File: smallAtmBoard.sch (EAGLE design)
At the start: 19 parts, among them IC1 ATMEGA-328P, IC2 7805, Y1 16MHz

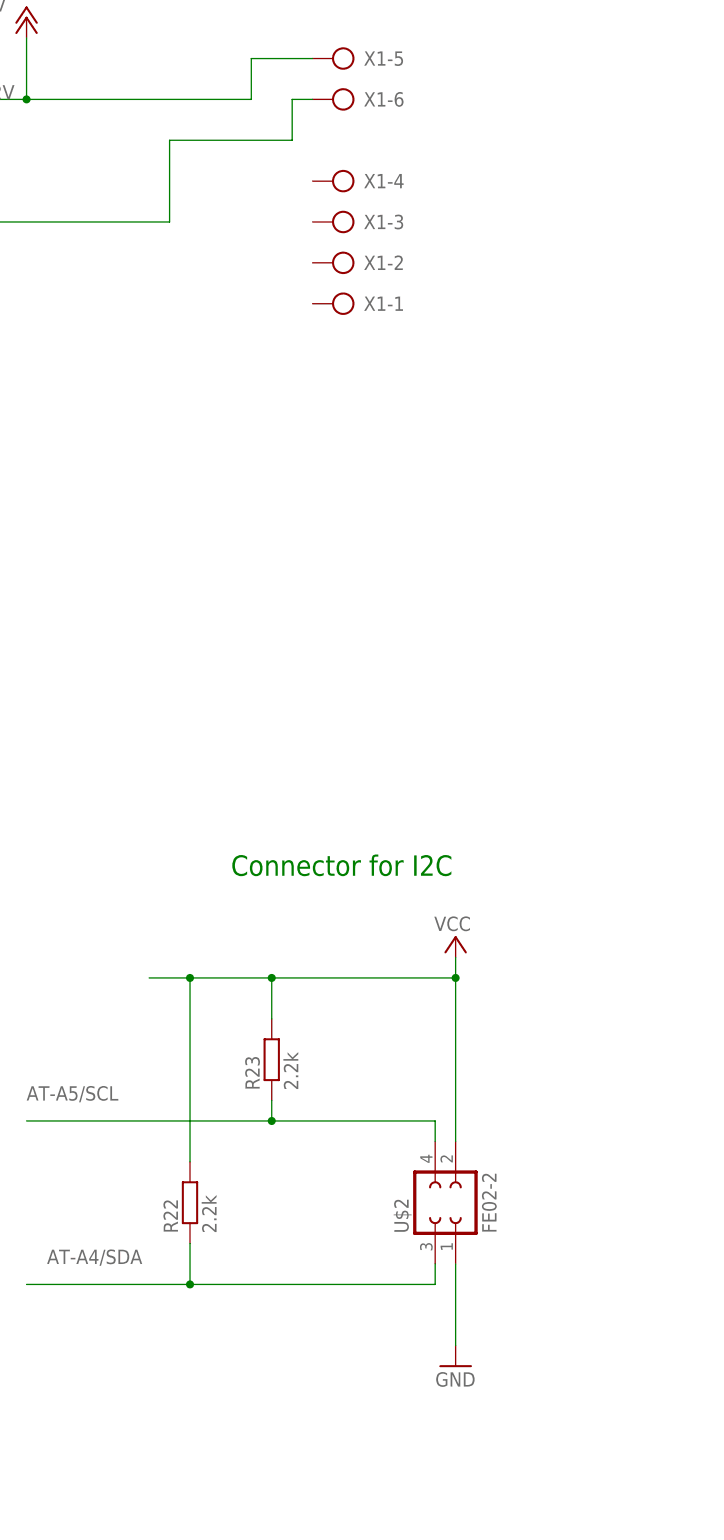
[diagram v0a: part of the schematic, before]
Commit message: remove i2c socket
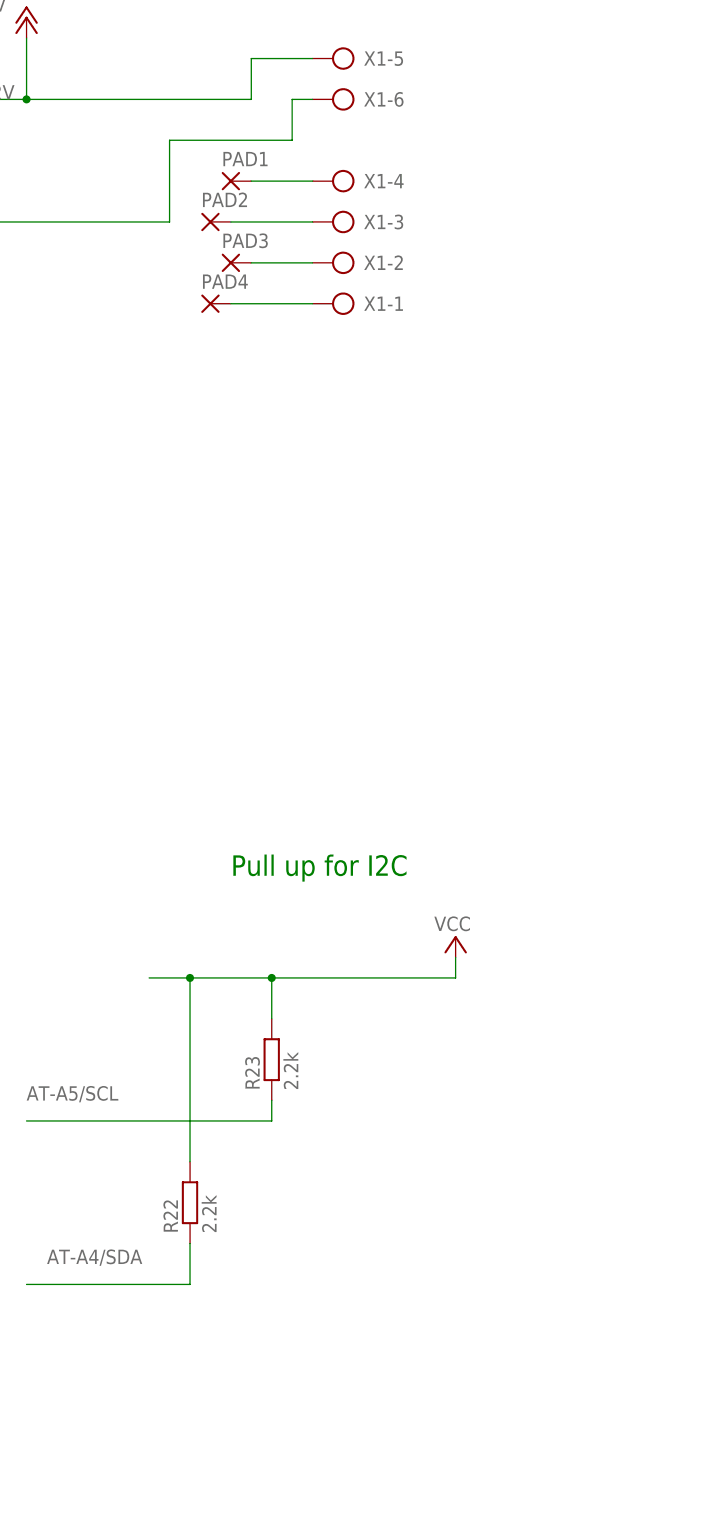
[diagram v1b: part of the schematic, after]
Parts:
- removed U$2: FE02-2, bauteile_jbt:FE02-2
- added PAD1, PAD2, PAD3, PAD4: (no value), bauteile_jbt:PAD1,6/0,8
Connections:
- new net N$115: PAD1.P, X1-4.KL
- new net N$119: PAD2.P, X1-3.KL
- new net N$123: PAD3.P, X1-2.KL
- new net N$175: PAD4.P, X1-1.KL
- net AT-A4/SDA: no longer U$2.3
- net AT-A5/SCL: no longer U$2.4
- net GND: no longer U$2.1
- net VCC: no longer U$2.2
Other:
- note added: "Pull up for I2C"
- note removed: "Connector for I2C"
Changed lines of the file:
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@@
 <part name="P+3" library="supply1" deviceset="VCC" device=""/>
 <part name="GND5" library="supply1" deviceset="GND" device=""/>
-<part name="GND6" library="supply1" deviceset="GND" device=""/>
 <part name="SV2" library="bauteile_jbt" deviceset="FE08-1" device="FE08-RAW"/>
-<part name="U$2" library="bauteile_jbt" deviceset="FE02-2" device=""/>
 <part name="P+1" library="supply1" deviceset="VCC" device=""/>
 <part name="X1" library="bauteile_jbt" deviceset="AK300/6" device=""/>
+<part name="PAD1" library="bauteile_jbt" deviceset="PAD1,6/0,8" device=""/>
+<part name="PAD2" library="bauteile_jbt" deviceset="PAD1,6/0,8" device=""/>
+<part name="PAD3" library="bauteile_jbt" deviceset="PAD1,6/0,8" device=""/>
+<part name="PAD4" library="bauteile_jbt" deviceset="PAD1,6/0,8" device=""/>
 </parts>
 <sheets>
@@
 <text x="181.102" y="241.3" size="2.54" layer="91">5V Supply</text>
 <text x="325.12" y="121.92" size="2.54" layer="91">Connector for Display / Keyboard </text>
-<text x="261.62" y="121.92" size="2.54" layer="91">Connector for I2C</text>
+<text x="261.62" y="121.92" size="2.54" layer="91">Pull up for I2C</text>
 </plain>
 <instances>
@@
 </instance>
 <instance part="GND5" gate="1" x="368.3" y="73.66"/>
-<instance part="GND6" gate="1" x="289.56" y="60.96"/>
 <instance part="SV2" gate="G$1" x="185.42" y="142.24" rot="R270"/>
-<instance part="U$2" gate="G$1" x="287.02" y="81.28" rot="R90"/>
 <instance part="P+1" gate="VCC" x="289.56" y="114.3" smashed="yes">
 <attribute name="VALUE" x="291.465" y="116.84" size="1.778" layer="96" rot="R180"/>
@@
 <instance part="X1" gate="-5" x="276.86" y="223.52" rot="R180"/>
 <instance part="X1" gate="-6" x="276.86" y="218.44" rot="R180"/>
+<instance part="PAD1" gate="P" x="261.62" y="208.28"/>
+<instance part="PAD2" gate="P" x="259.08" y="203.2"/>
+<instance part="PAD3" gate="P" x="261.62" y="198.12"/>
+<instance part="PAD4" gate="P" x="259.08" y="193.04"/>
 </instances>
 <busses>
@@
 <wire x1="368.3" y1="76.2" x2="358.14" y2="76.2" width="0.1524" layer="91"/>
 <wire x1="358.14" y1="76.2" x2="358.14" y2="81.28" width="0.1524" layer="91"/>
-</segment>
-<segment>
-<pinref part="GND6" gate="1" pin="GND"/>
-<pinref part="U$2" gate="G$1" pin="1"/>
-<wire x1="289.56" y1="63.5" x2="289.56" y2="73.66" width="0.1524" layer="91"/>
 </segment>
 </net>
@@
 </segment>
 <segment>
-<pinref part="U$2" gate="G$1" pin="2"/>
 <pinref part="P+1" gate="VCC" pin="VCC"/>
-<wire x1="289.56" y1="88.9" x2="289.56" y2="109.22" width="0.1524" layer="91"/>
 <wire x1="289.56" y1="109.22" x2="289.56" y2="111.76" width="0.1524" layer="91"/>
 <wire x1="289.56" y1="109.22" x2="266.7" y2="109.22" width="0.1524" layer="91"/>
@@
 <wire x1="256.54" y1="86.36" x2="256.54" y2="109.22" width="0.1524" layer="91"/>
 <junction x="256.54" y="109.22"/>
-<junction x="289.56" y="109.22"/>
 </segment>
 </net>
@@
 <segment>
 <label x="238.76" y="73.66" size="1.778" layer="95"/>
-<wire x1="287.02" y1="71.12" x2="256.54" y2="71.12" width="0.1524" layer="91"/>
-<pinref part="U$2" gate="G$1" pin="3"/>
-<wire x1="287.02" y1="73.66" x2="287.02" y2="71.12" width="0.1524" layer="91"/>
 <wire x1="256.54" y1="71.12" x2="236.22" y2="71.12" width="0.1524" layer="91"/>
-<junction x="256.54" y="71.12"/>
 <pinref part="R22" gate="G$1" pin="1"/>
 <wire x1="256.54" y1="76.2" x2="256.54" y2="71.12" width="0.1524" layer="91"/>
@@
 <wire x1="266.7" y1="91.44" x2="236.22" y2="91.44" width="0.1524" layer="91"/>
 <label x="236.22" y="93.98" size="1.778" layer="95"/>
-<wire x1="287.02" y1="91.44" x2="266.7" y2="91.44" width="0.1524" layer="91"/>
-<pinref part="U$2" gate="G$1" pin="4"/>
-<wire x1="287.02" y1="91.44" x2="287.02" y2="88.9" width="0.1524" layer="91"/>
-<junction x="266.7" y="91.44"/>
 </segment>
 </net>
@@
 </segment>
 </net>
+<net name="N$115" class="0">
+<segment>
+<pinref part="PAD1" gate="P" pin="P"/>
+<pinref part="X1" gate="-4" pin="KL"/>
+<wire x1="264.16" y1="208.28" x2="271.78" y2="208.28" width="0.1524" layer="91"/>
+</segment>
+</net>
+<net name="N$119" class="0">
+<segment>
+<pinref part="PAD2" gate="P" pin="P"/>
+<pinref part="X1" gate="-3" pin="KL"/>
+<wire x1="261.62" y1="203.2" x2="271.78" y2="203.2" width="0.1524" layer="91"/>
+</segment>
+</net>
+<net name="N$123" class="0">
+<segment>
+<pinref part="PAD3" gate="P" pin="P"/>
+<pinref part="X1" gate="-2" pin="KL"/>
+<wire x1="264.16" y1="198.12" x2="271.78" y2="198.12" width="0.1524" layer="91"/>
+</segment>
+</net>
+<net name="N$175" class="0">
+<segment>
+<pinref part="PAD4" gate="P" pin="P"/>
+<pinref part="X1" gate="-1" pin="KL"/>
+<wire x1="261.62" y1="193.04" x2="271.78" y2="193.04" width="0.1524" layer="91"/>
+</segment>
+</net>

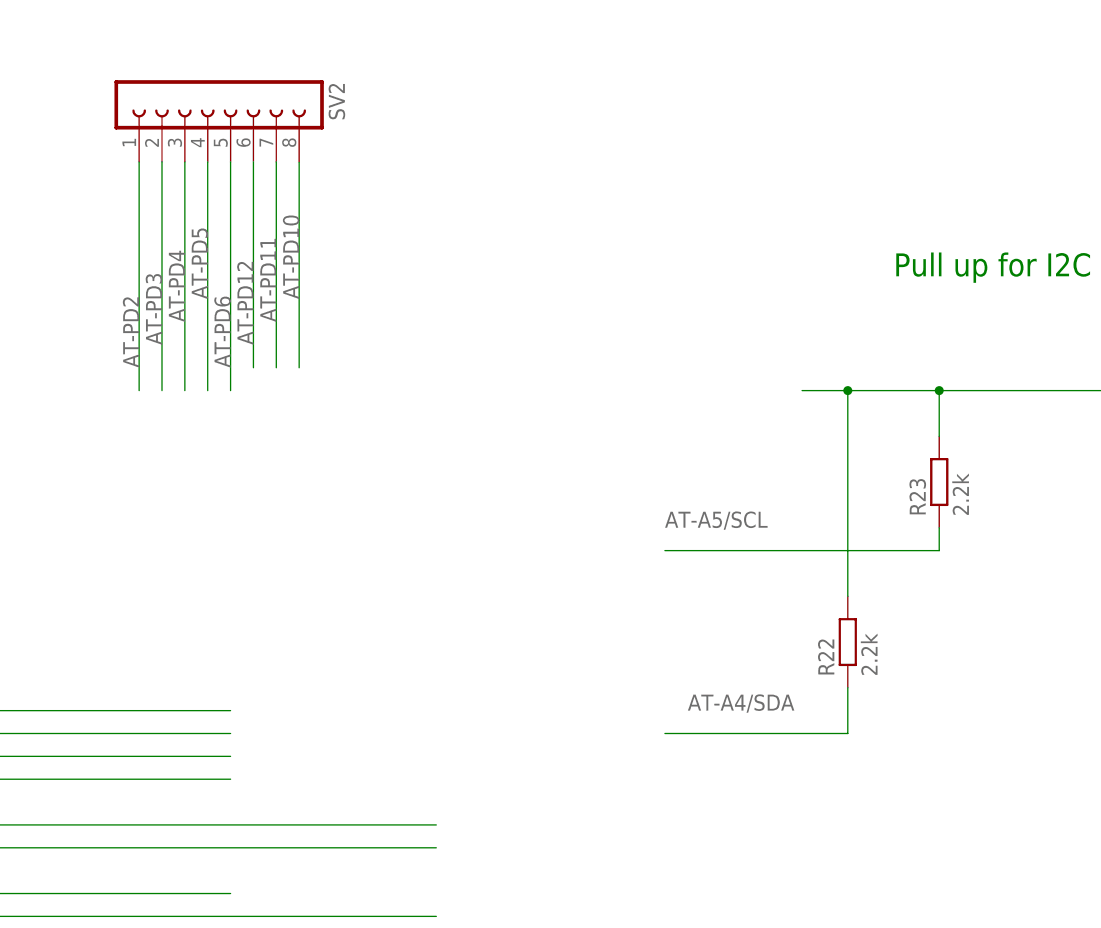
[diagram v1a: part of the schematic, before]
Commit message: exchange D10 and D12, no i2c
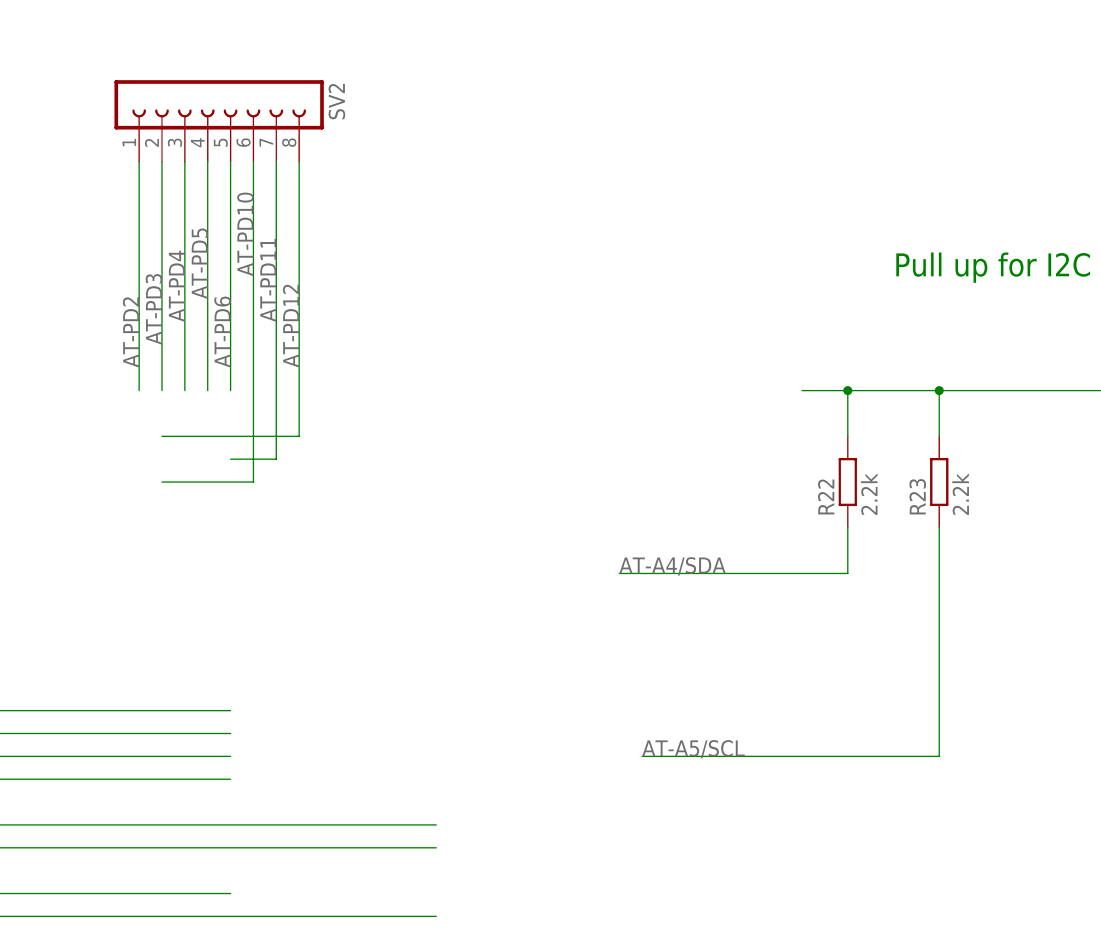
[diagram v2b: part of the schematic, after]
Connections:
- net AT-PD10: now also SV2.6; no longer SV2.8
- net AT-PD12: now also SV2.8; no longer SV2.6
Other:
- moved on the sheet: R22
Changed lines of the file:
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@@
 <instance part="IC2" gate="G$1" x="210.82" y="218.44" rot="MR0"/>
 <instance part="GND9" gate="1" x="180.34" y="195.58"/>
-<instance part="R22" gate="G$1" x="256.54" y="81.28" rot="R90"/>
+<instance part="R22" gate="G$1" x="256.54" y="99.06" rot="R90"/>
 <instance part="R23" gate="G$1" x="266.7" y="99.06" rot="R90"/>
 <instance part="SV3" gate="G$1" x="137.16" y="142.24" rot="R270"/>
@@
 <junction x="266.7" y="109.22"/>
 <pinref part="R22" gate="G$1" pin="2"/>
-<wire x1="256.54" y1="86.36" x2="256.54" y2="109.22" width="0.1524" layer="91"/>
+<wire x1="256.54" y1="104.14" x2="256.54" y2="109.22" width="0.1524" layer="91"/>
 <junction x="256.54" y="109.22"/>
 </segment>
@@
 </segment>
 <segment>
-<label x="238.76" y="73.66" size="1.778" layer="95"/>
-<wire x1="256.54" y1="71.12" x2="236.22" y2="71.12" width="0.1524" layer="91"/>
+<label x="231.14" y="88.9" size="1.778" layer="95"/>
 <pinref part="R22" gate="G$1" pin="1"/>
-<wire x1="256.54" y1="76.2" x2="256.54" y2="71.12" width="0.1524" layer="91"/>
+<wire x1="256.54" y1="88.9" x2="231.14" y2="88.9" width="0.1524" layer="91"/>
+<wire x1="256.54" y1="93.98" x2="256.54" y2="88.9" width="0.1524" layer="91"/>
 </segment>
 </net>
@@
 </segment>
 <segment>
-<pinref part="SV2" gate="G$1" pin="8"/>
-<wire x1="195.58" y1="134.62" x2="195.58" y2="111.76" width="0.1524" layer="91"/>
-<label x="195.58" y="119.38" size="1.778" layer="95" rot="R90"/>
+<label x="190.5" y="121.92" size="1.778" layer="95" rot="R90"/>
+<wire x1="190.5" y1="99.06" x2="180.34" y2="99.06" width="0.1524" layer="91"/>
+<pinref part="SV2" gate="G$1" pin="6"/>
+<wire x1="190.5" y1="99.06" x2="190.5" y2="134.62" width="0.1524" layer="91"/>
 </segment>
 </net>
@@
 </segment>
 <segment>
-<pinref part="SV2" gate="G$1" pin="6"/>
-<wire x1="190.5" y1="134.62" x2="190.5" y2="111.76" width="0.1524" layer="91"/>
-<label x="190.5" y="114.3" size="1.778" layer="95" rot="R90"/>
+<label x="195.58" y="111.76" size="1.778" layer="95" rot="R90"/>
+<wire x1="195.58" y1="104.14" x2="180.34" y2="104.14" width="0.1524" layer="91"/>
+<pinref part="SV2" gate="G$1" pin="8"/>
+<wire x1="195.58" y1="104.14" x2="195.58" y2="134.62" width="0.1524" layer="91"/>
 </segment>
 </net>
@@
 <segment>
 <pinref part="SV2" gate="G$1" pin="7"/>
-<wire x1="193.04" y1="134.62" x2="193.04" y2="111.76" width="0.1524" layer="91"/>
+<wire x1="193.04" y1="134.62" x2="193.04" y2="101.6" width="0.1524" layer="91"/>
 <label x="193.04" y="116.84" size="1.778" layer="95" rot="R90"/>
+<wire x1="193.04" y1="101.6" x2="187.96" y2="101.6" width="0.1524" layer="91"/>
 </segment>
 </net>
@@
 <segment>
 <pinref part="R23" gate="G$1" pin="1"/>
-<wire x1="266.7" y1="93.98" x2="266.7" y2="91.44" width="0.1524" layer="91"/>
-<wire x1="266.7" y1="91.44" x2="236.22" y2="91.44" width="0.1524" layer="91"/>
-<label x="236.22" y="93.98" size="1.778" layer="95"/>
-</segment>
-</net>
+<wire x1="266.7" y1="93.98" x2="266.7" y2="68.58" width="0.1524" layer="91"/>
+<label x="233.68" y="68.58" size="1.778" layer="95"/>
+<wire x1="266.7" y1="68.58" x2="233.68" y2="68.58" width="0.1524" layer="91"/>
+</segment>
+</net>
